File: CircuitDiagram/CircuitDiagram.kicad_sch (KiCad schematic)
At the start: 24 parts

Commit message: Update to circuit diagram
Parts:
- removed D? (x4): LED_PAD_9V, symbol CustomCircuitLib:LED_PAD_9V
- removed MK1: Microphone, symbol Device:Microphone
- removed V1: +12V, symbol CustomCircuitLib:Voltage_Source
- added R10, R9: R330, symbol Device:R
- added V2: +12V, symbol CustomCircuitLib:Voltage_Source
- R1, R2, R3, R4: value R1 -> R3
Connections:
- net at R1.2, R2.2, R3.2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: now also R9.1
- net at Q?.2 (G), R8.1: now also A1.26 (D11); no longer A1.24 (D9)
- net at A1.29 (GND), Q?.1 (Source), Q?.1 (Source)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: now also R10.2
- net at Q?.2 (G), R7.1: now also A1.25 (D10); no longer A1.22 (D7)
- net at V1. (VPP): now also A1.5 (+5V)
- net at A1.27 (D12): no longer V1. (VPP)
- net at A1.28 (D13): no longer V1. (VPP)
- net at Q?.2 (G), R6.1: now also A1.24 (D9); no longer A1.20 (D5)
- net at A1.17 (D2): now also V1. (VPP)
- net at Q?.2 (G), R5.1: now also A1.21 (D6); no longer A1.18 (D3)
- net at A1.8 (VIN): now also R10.1, R9.2
- new net: A1.18 (D3), V1. (VPP)
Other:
- note removed: "GND"
- note removed: "Left"
- note removed: "Right"

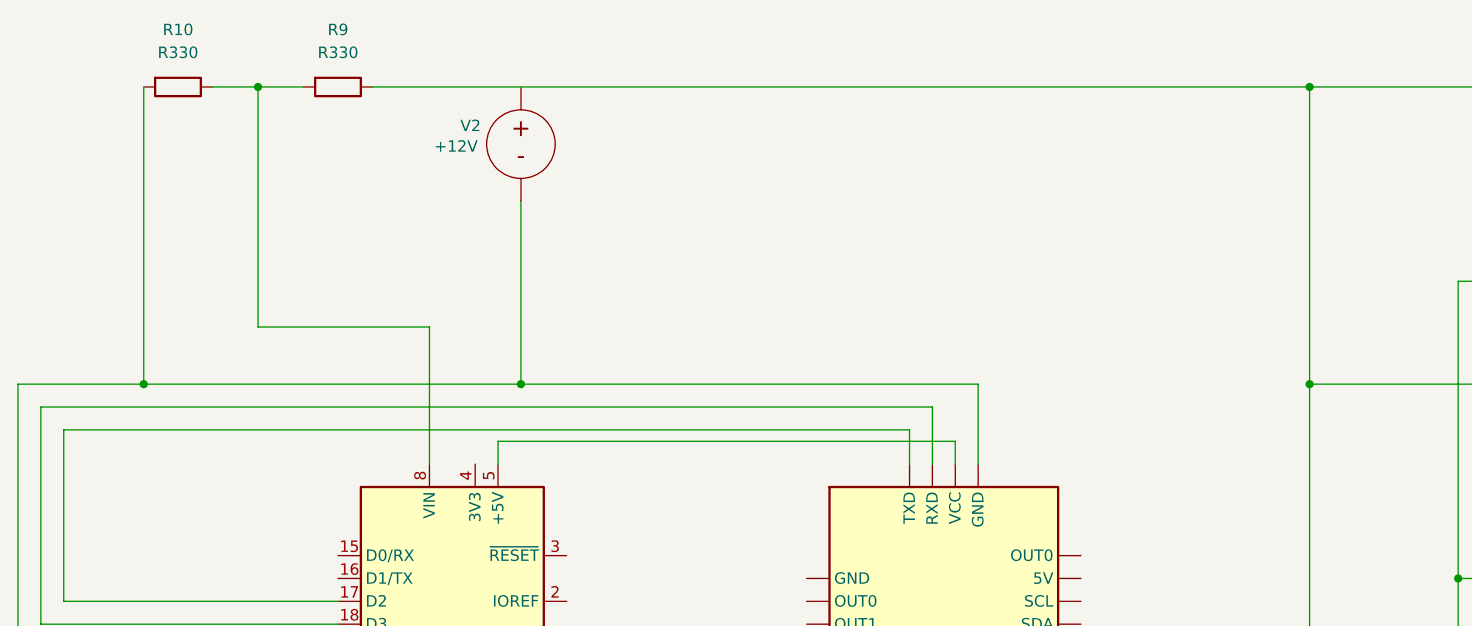
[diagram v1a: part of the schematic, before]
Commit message: Removed voltage divider, directly connect 12V to Arduino
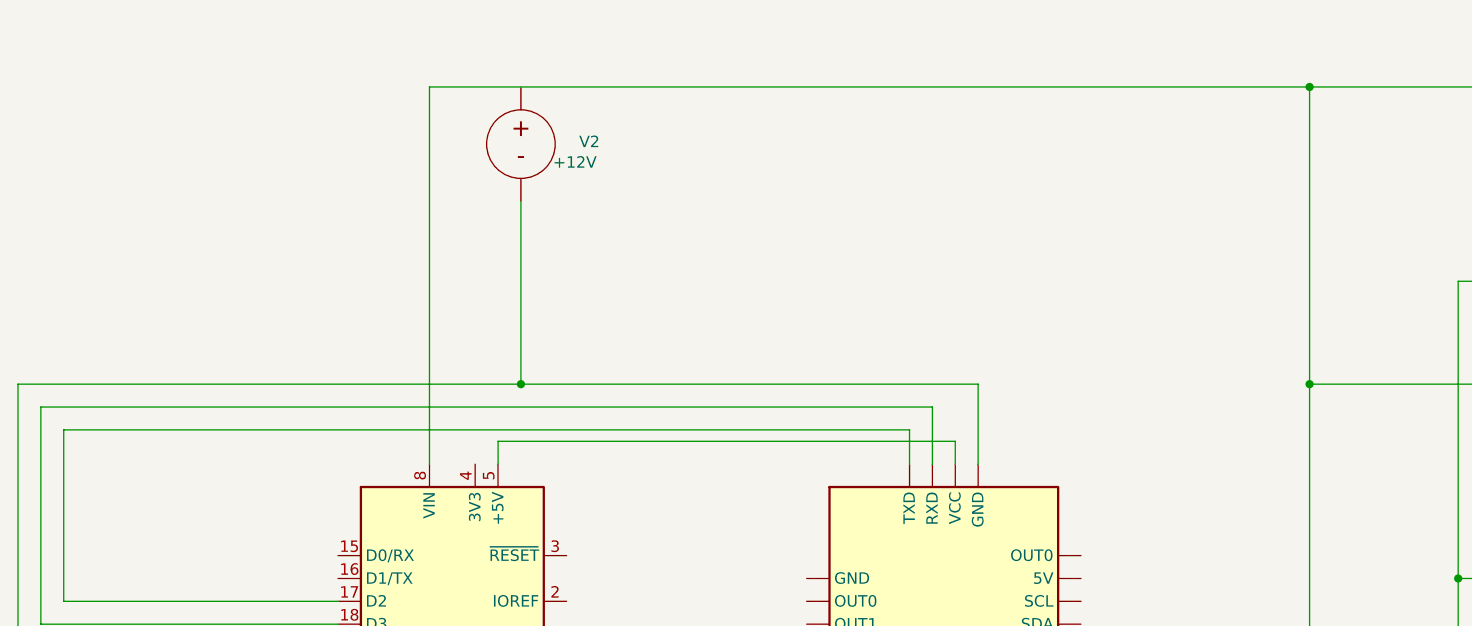
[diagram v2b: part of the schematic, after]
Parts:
- removed R10, R9: R330, symbol Device:R
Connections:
- net at R1.2, R2.2, R3.2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: now also A1.8 (VIN)
- net at V1. (VPP): now also A1.5 (+5V)
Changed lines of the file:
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@@
-	)
-	(junction
-		(at 44.45 59.69)
-		(diameter 0)
-		(color 0 0 0 0)
 	)
 	(junction
@@
 	)
 	(junction
-		(at 57.15 26.67)
-		(diameter 0)
-		(color 0 0 0 0)
-	)
-	(junction
 		(at 113.03 138.43)
 		(diameter 0)
@@
 	(wire
 		(pts
+			(xy 35.56 83.82) (xy 66.04 83.82)
+		)
+		(stroke
+			(width 0)
+			(type default)
+			(color 132 132 132 1)
+		)
+	)
+	(wire
+		(pts
 			(xy 35.56 83.82) (xy 35.56 64.77)
 		)
@@
 	(wire
 		(pts
-			(xy 52.07 26.67) (xy 57.15 26.67)
-		)
-		(stroke
-			(width 0)
-			(type default)
-		)
-	)
-	(wire
-		(pts
 			(xy 236.22 125.73) (xy 236.22 129.54)
 		)
@@
 	(wire
 		(pts
-			(xy 44.45 26.67) (xy 44.45 59.69)
-		)
-		(stroke
-			(width 0)
-			(type default)
-		)
-	)
-	(wire
-		(pts
 			(xy 219.71 81.28) (xy 190.5 81.28)
 		)
@@
 	(wire
 		(pts
+			(xy 76.2 26.67) (xy 173.99 26.67)
+		)
+		(stroke
+			(width 0)
+			(type default)
+		)
+	)
+	(wire
+		(pts
 			(xy 223.52 53.34) (xy 223.52 34.29)
 		)
@@
 	(wire
 		(pts
-			(xy 76.2 53.34) (xy 76.2 68.58)
+			(xy 76.2 26.67) (xy 76.2 68.58)
 		)
 		(stroke
@@
 	(wire
 		(pts
+			(xy 33.02 86.36) (xy 66.04 86.36)
+		)
+		(stroke
+			(width 0)
+			(type default)
+			(color 132 132 132 1)
+		)
+	)
+	(wire
+		(pts
 			(xy 76.2 121.92) (xy 76.2 129.54)
 		)
@@
 	(wire
 		(pts
-			(xy 69.85 26.67) (xy 173.99 26.67)
-		)
-		(stroke
-			(width 0)
-			(type default)
-		)
-	)
-	(wire
-		(pts
-			(xy 33.02 86.36) (xy 66.04 86.36)
-		)
-		(stroke
-			(width 0)
-			(type default)
-		)
-	)
-	(wire
-		(pts
 			(xy 219.71 80.01) (xy 219.71 81.28)
 		)
@@
 	(wire
 		(pts
-			(xy 57.15 26.67) (xy 62.23 26.67)
-		)
-		(stroke
-			(width 0)
-			(type default)
-		)
-	)
-	(wire
-		(pts
 			(xy 219.71 114.3) (xy 190.5 114.3)
 		)
@@
 	(wire
 		(pts
-			(xy 57.15 26.67) (xy 57.15 53.34)
-		)
-		(stroke
-			(width 0)
-			(type default)
-		)
-	)
-	(wire
-		(pts
 			(xy 223.52 119.38) (xy 223.52 100.33)
 		)
@@
 	(wire
 		(pts
-			(xy 57.15 53.34) (xy 76.2 53.34)
-		)
-		(stroke
-			(width 0)
-			(type default)
-		)
-	)
-	(wire
-		(pts
-			(xy 44.45 59.69) (xy 86.36 59.69)
+			(xy 30.48 59.69) (xy 86.36 59.69)
 		)
 		(stroke
@@
 	(wire
 		(pts
-			(xy 35.56 83.82) (xy 66.04 83.82)
-		)
-		(stroke
-			(width 0)
-			(type default)
-		)
-	)
-	(wire
-		(pts
 			(xy 50.8 133.35) (xy 107.95 133.35)
 		)
@@
 		(pts
 			(xy 190.5 81.28) (xy 190.5 114.3)
-		)
-		(stroke
-			(width 0)
-			(type default)
-		)
-	)
-	(wire
-		(pts
-			(xy 30.48 59.69) (xy 44.45 59.69)
 		)
 		(stroke
@@
 	)
 	(symbol
-		(lib_id "Device:R")
-		(at 48.26 26.67 270)
-		(unit 1)
-		(exclude_from_sim no)
-		(in_bom yes)
-		(on_board yes)
-		(dnp no)
-		(property "Reference" "R10"
-			(at 48.26 20.32 90)
-			(effects
-				(font
-					(size 1.27 1.27)
-				)
-			)
-		)
-		(property "Value" "R330"
-			(at 48.26 22.86 90)
-			(effects
-				(font
-					(size 1.27 1.27)
-				)
-			)
-		)
-		(property "Footprint" ""
-			(at 48.26 24.892 90)
-			(effects
-				(font
-					(size 1.27 1.27)
-				)
-				(hide yes)
-			)
-		)
-		(property "Datasheet" "~"
-			(at 48.26 26.67 0)
-			(effects
-				(font
-					(size 1.27 1.27)
-				)
-				(hide yes)
-			)
-		)
-		(property "Description" ""
-			(at 48.26 26.67 0)
-			(effects
-				(font
-					(size 1.27 1.27)
-				)
-				(hide yes)
-			)
-		)
-		(pin "1"
-		)
-		(pin "2"
-		)
-		(instances
-			(project "CircuitDiagram"
-				(path "/b4bf23ee-e5c4-404a-ad1d-c484e36cae28"
-					(reference "R10")
-					(unit 1)
-				)
-			)
-		)
-	)
-	(symbol
 		(lib_id "CustomCircuitLib:LED_PAD_9V")
 		(at 232.41 147.32 90)
@@
 		(dnp no)
 		(property "Reference" "V2"
-			(at 80.772 30.988 0)
+			(at 93.98 32.766 0)
 			(effects
 				(font
@@
 		)
 		(property "Value" "+12V"
-			(at 76.708 33.274 0)
+			(at 89.916 35.052 0)
 			(effects
 				(font
@@
 					(unit 1)
 				)
-			)
-		)
-	)
-	(symbol
-		(lib_id "Device:R")
-		(at 66.04 26.67 270)
-		(unit 1)
-		(exclude_from_sim no)
-		(in_bom yes)
-		(on_board yes)
-		(dnp no)
-		(property "Reference" "R9"
-			(at 66.04 20.32 90)
-			(effects
-				(font
-					(size 1.27 1.27)
-				)
-			)
-		)
-		(property "Value" "R330"
-			(at 66.04 22.86 90)
-			(effects
-				(font
-					(size 1.27 1.27)
-				)
-			)
-		)
-		(property "Footprint" ""
-			(at 66.04 24.892 90)
-			(effects
-				(font
-					(size 1.27 1.27)
-				)
-				(hide yes)
-			)
-		)
-		(property "Datasheet" "~"
-			(at 66.04 26.67 0)
-			(effects
-				(font
-					(size 1.27 1.27)
-				)
-				(hide yes)
-			)
-		)
-		(property "Description" ""
-			(at 66.04 26.67 0)
-			(effects
-				(font
-					(size 1.27 1.27)
-				)
-				(hide yes)
-			)
-		)
-		(pin "1"
-		)
-		(pin "2"
-		)
-		(instances
-			(project "CircuitDiagram"
-				(path "/b4bf23ee-e5c4-404a-ad1d-c484e36cae28"
-					(reference "R9")
-					(unit 1)
-				)

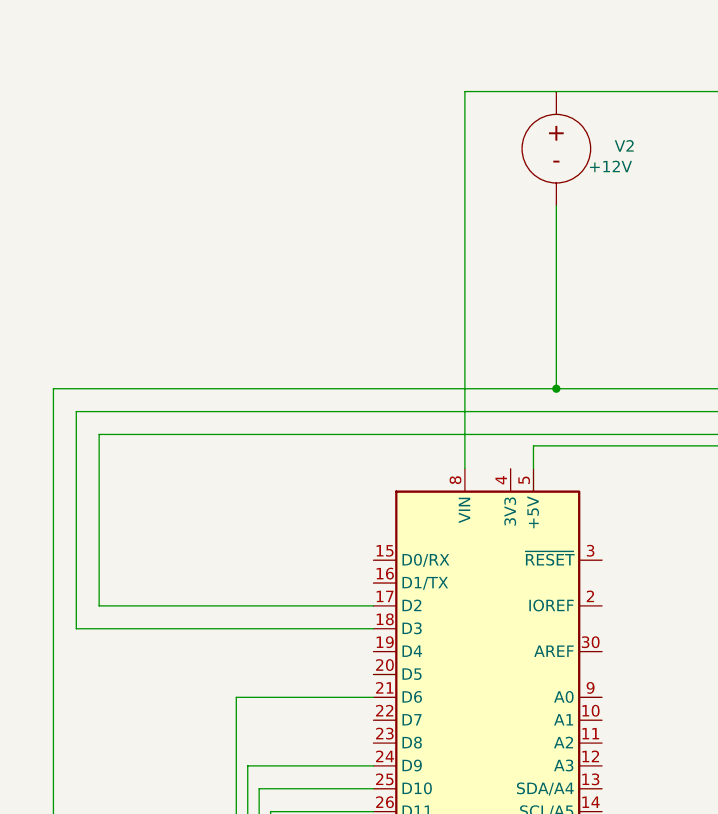
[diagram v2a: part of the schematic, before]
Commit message: Updated Circuit Diagram to include motion sensor
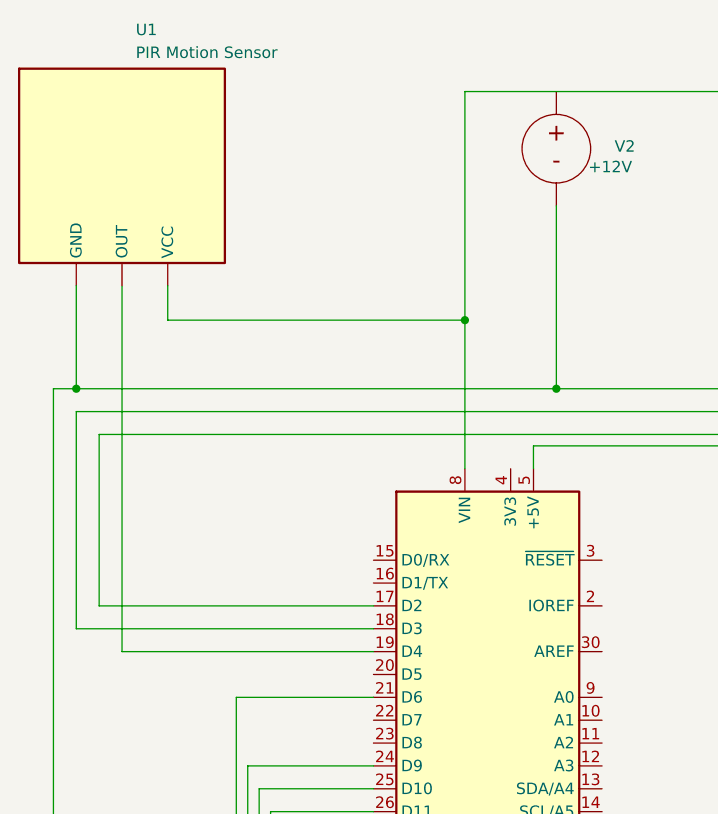
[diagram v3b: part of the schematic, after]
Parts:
- added U1: PIR Motion Sensor, Package_LGA:LGA-28_5.2x3.8mm_P0.5mm, symbol Sensor_Motion:BMF055
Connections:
- net at A1.8 (VIN), R1.2, R2.2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: now also U1. (VCC)
- net at A1.29 (GND), Q?.1 (Source), Q?.1 (Source)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: now also U1. (VCC)
- net at V1. (VPP): now also A1.5 (+5V)
- net at A1.19 (D4): now also U1. (VCC)
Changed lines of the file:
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@@
+	)
+	(junction
+		(at 76.2 52.07)
+		(diameter 0)
+		(color 0 0 0 0)
 	)
 	(junction
@@
 	)
 	(junction
+		(at 33.02 59.69)
+		(diameter 0)
+		(color 0 0 0 0)
+	)
+	(junction
 		(at 110.49 135.89)
 		(diameter 0)
@@
 	(wire
 		(pts
+			(xy 66.04 88.9) (xy 38.1 88.9)
+		)
+		(stroke
+			(width 0)
+			(type default)
+			(color 132 132 132 1)
+		)
+	)
+	(wire
+		(pts
+			(xy 33.02 48.26) (xy 33.02 59.69)
+		)
+		(stroke
+			(width 0)
+			(type default)
+		)
+	)
+	(wire
+		(pts
 			(xy 219.71 81.28) (xy 190.5 81.28)
 		)
@@
 	(wire
 		(pts
+			(xy 30.48 59.69) (xy 33.02 59.69)
+		)
+		(stroke
+			(width 0)
+			(type default)
+		)
+	)
+	(wire
+		(pts
 			(xy 223.52 53.34) (xy 223.52 34.29)
 		)
@@
 	(wire
 		(pts
-			(xy 76.2 26.67) (xy 76.2 68.58)
+			(xy 76.2 26.67) (xy 76.2 52.07)
 		)
 		(stroke
@@
 	(wire
 		(pts
+			(xy 43.18 48.26) (xy 43.18 52.07)
+		)
+		(stroke
+			(width 0)
+			(type default)
+		)
+	)
+	(wire
+		(pts
 			(xy 190.5 114.3) (xy 190.5 146.05)
 		)
@@
 	(wire
 		(pts
+			(xy 76.2 52.07) (xy 76.2 68.58)
+		)
+		(stroke
+			(width 0)
+			(type default)
+		)
+	)
+	(wire
+		(pts
 			(xy 54.61 140.97) (xy 115.57 140.97)
 		)
@@
 	(wire
 		(pts
+			(xy 43.18 52.07) (xy 76.2 52.07)
+		)
+		(stroke
+			(width 0)
+			(type default)
+		)
+	)
+	(wire
+		(pts
 			(xy 190.5 146.05) (xy 88.9 146.05)
 		)
@@
 	(wire
 		(pts
-			(xy 30.48 59.69) (xy 86.36 59.69)
-		)
-		(stroke
-			(width 0)
-			(type default)
-		)
-	)
-	(wire
-		(pts
 			(xy 219.71 46.99) (xy 219.71 48.26)
 		)
@@
 	(wire
 		(pts
+			(xy 33.02 59.69) (xy 86.36 59.69)
+		)
+		(stroke
+			(width 0)
+			(type default)
+		)
+	)
+	(wire
+		(pts
 			(xy 199.39 138.43) (xy 199.39 107.95)
 		)
@@
 			(width 0)
 			(type default)
+		)
+	)
+	(wire
+		(pts
+			(xy 38.1 88.9) (xy 38.1 48.26)
+		)
+		(stroke
+			(width 0)
+			(type default)
+			(color 132 132 132 1)
 		)
 	)
@@
 					(unit 1)
 				)
+			)
+		)
+	)
+	(symbol
+		(lib_id "Sensor_Motion:BMF055")
+		(at 38.1 25.4 0)
+		(unit 1)
+		(exclude_from_sim no)
+		(in_bom yes)
+		(on_board yes)
+		(dnp no)
+		(fields_autoplaced yes)
+		(property "Reference" "U1"
+			(at 39.624 19.812 0)
+			(effects
+				(font
+					(size 1.27 1.27)
+				)
+				(justify left)
+			)
+		)
+		(property "Value" "PIR Motion Sensor"
+			(at 39.624 22.352 0)
+			(effects
+				(font
+					(size 1.27 1.27)
+				)
+				(justify left)
+			)
+		)
+		(property "Footprint" "Package_LGA:LGA-28_5.2x3.8mm_P0.5mm"
+			(at 77.978 -5.334 0)
+			(effects
+				(font
+					(size 1.27 1.27)
+				)
+				(justify left)
+				(hide yes)
+			)
+		)
+		(property "Datasheet" "https://www.bosch-sensortec.com/media/boschsensortec/downloads/datasheets/bst-bmf055-ds000.pdf"
+			(at 116.84 0.254 0)
+			(effects
+				(font
+					(size 1.27 1.27)
+				)
+				(hide yes)
+			)
+		)
+		(property "Description" "Custom programmable 9-axis motion sensor"
+			(at 96.266 5.334 0)
+			(effects
+				(font
+					(size 1.27 1.27)
+				)
+				(hide yes)
+			)
+		)
+		(pin ""
+		)
+		(pin ""
+		)
+		(pin ""
+		)
+		(instances
+			(project "CircuitDiagram"
+				(path "/b4bf23ee-e5c4-404a-ad1d-c484e36cae28"
+					(reference "U1")
+					(unit 1)
+				)
